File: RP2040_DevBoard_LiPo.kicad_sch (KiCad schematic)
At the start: 56 parts, among them J1 USB_C_Receptacle_USB2.0, J2 Conn_01x18, J3 Conn_01x18, SW1 SW_Push, SW2 SW_Push, U1 W25Q128JVS, U2 USBLC6-2SC6, U3 RP2040, Y1 Crystal_GND23

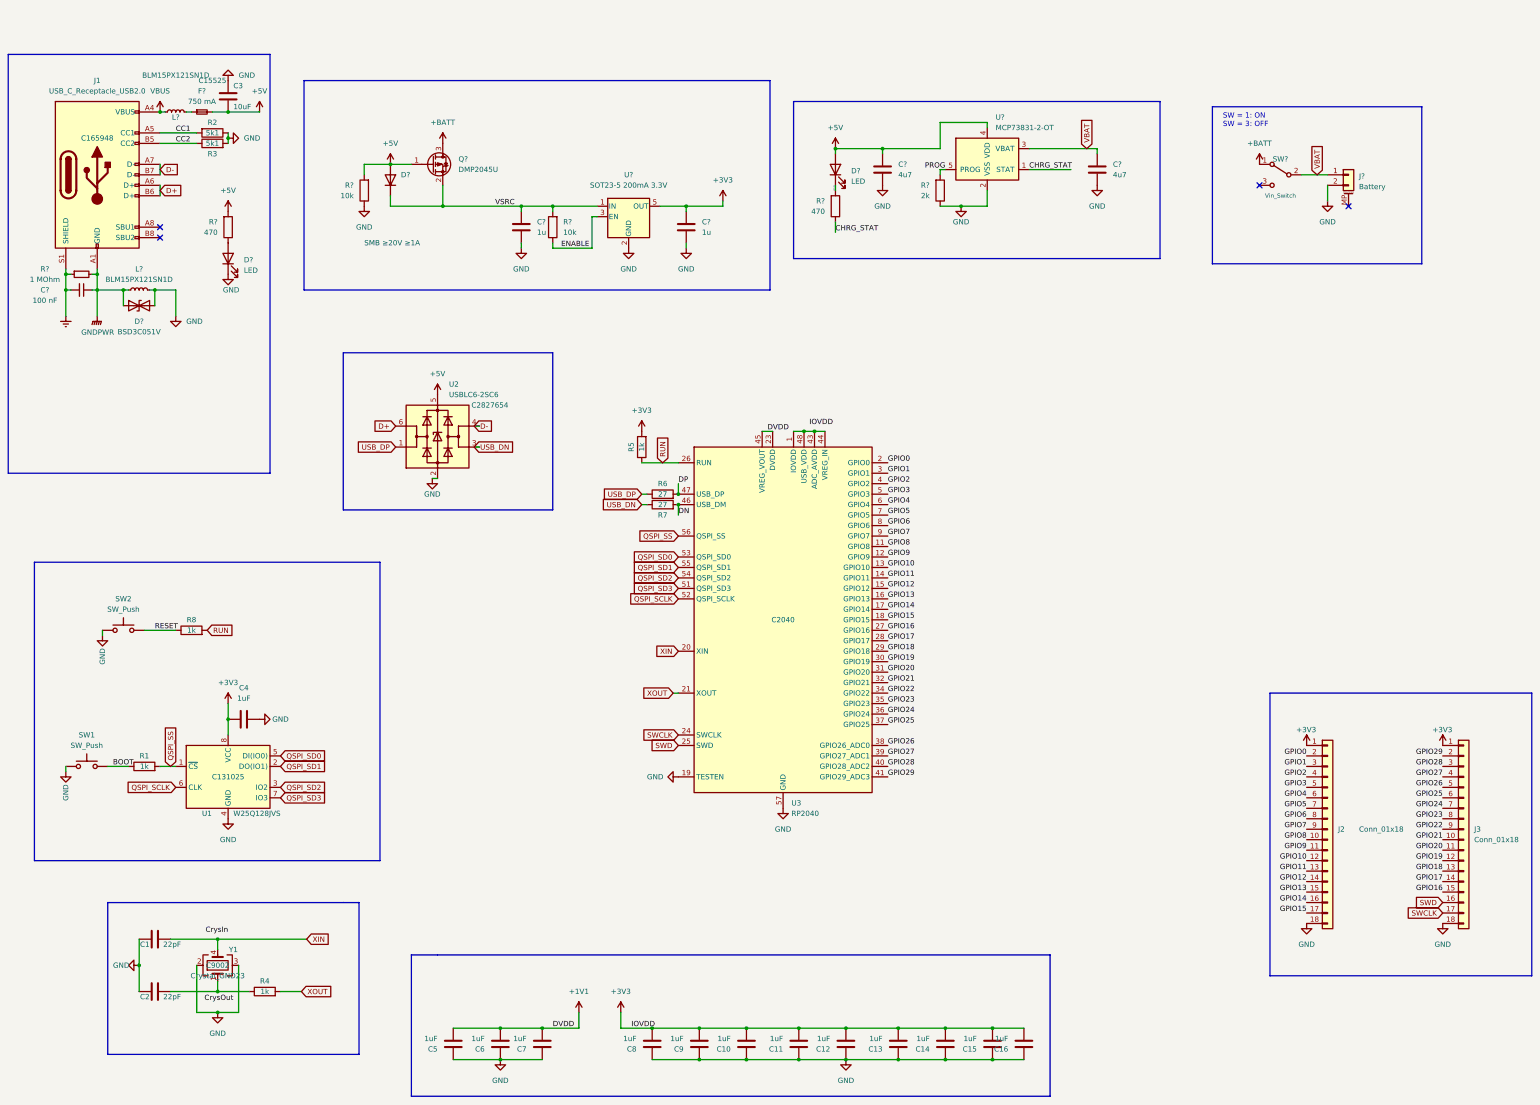
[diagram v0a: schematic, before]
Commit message: added missing 3v3 arrow, changed some footprints
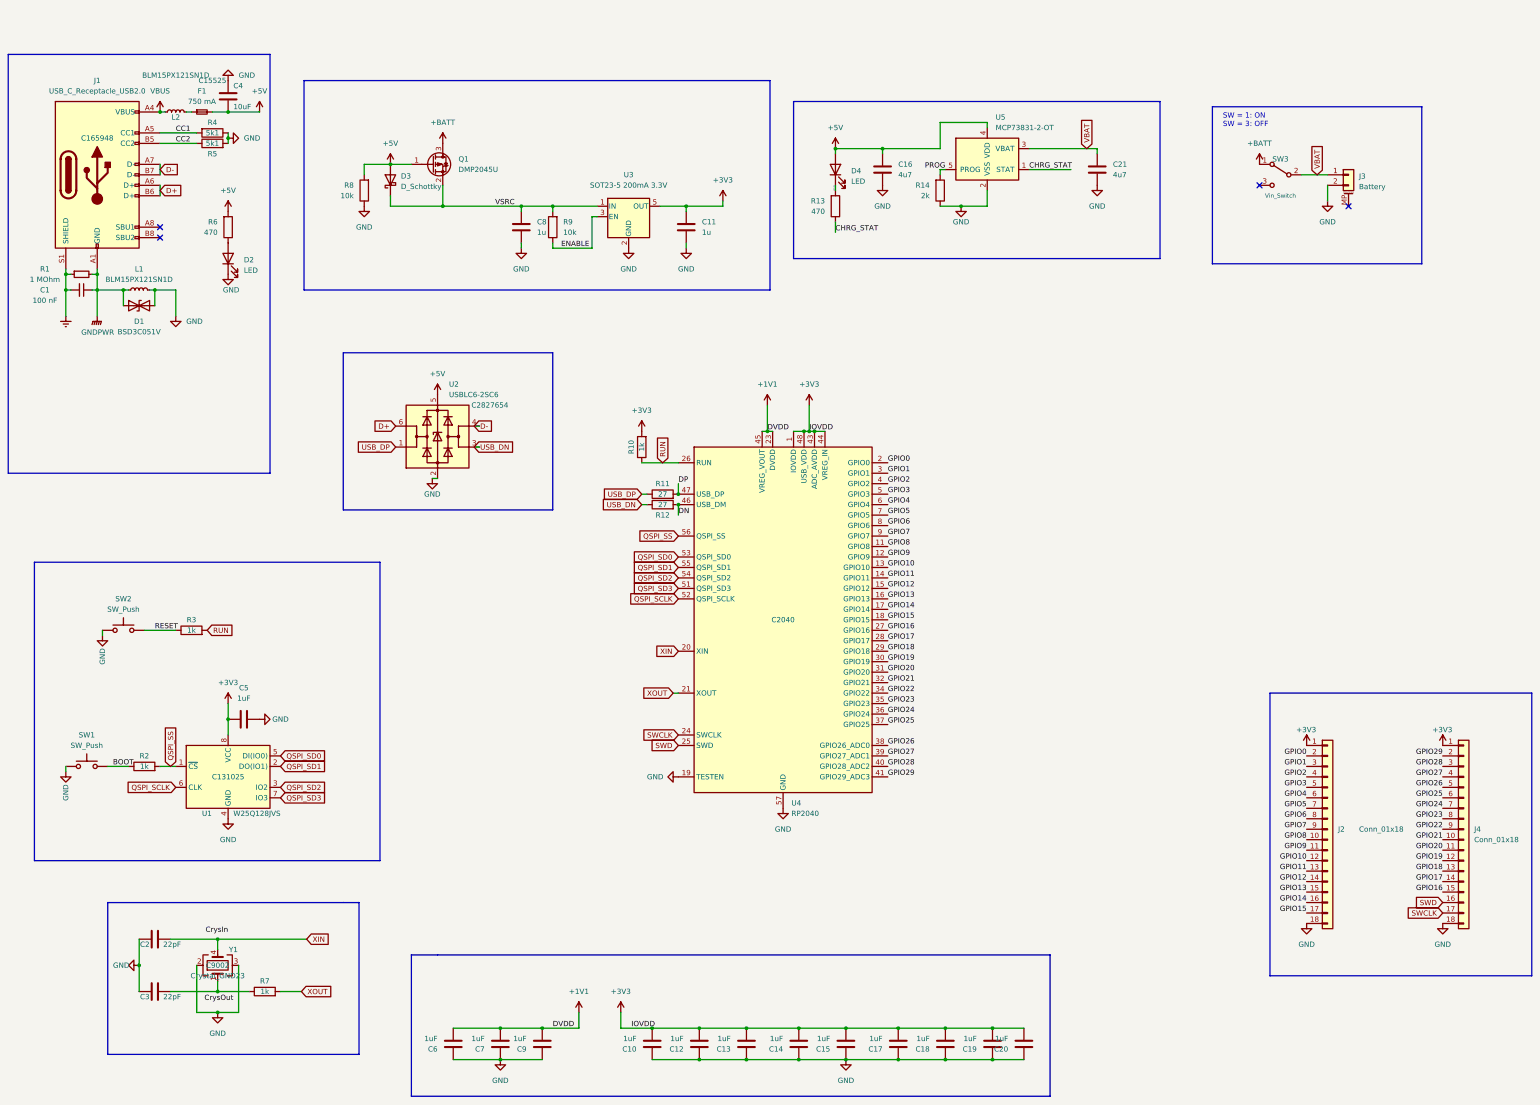
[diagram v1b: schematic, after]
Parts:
- removed D?: SMB ≥20V ≥1A, Diode_SMD:D_1206_3216Metric_Pad1.42x1.75mm_HandSolder, symbol Device:D
- added D3: D_Schottky, Diode_SMD:D_0603_1608Metric, symbol Device:D_Schottky
- C1: renamed from C?; footprint Capacitor_SMD:C_0402_1005Metric -> Diode_SMD:D_0603_1608Metric
- C11, C16, C21, C8: renamed from C?; footprint Capacitor_SMD:C_0805_2012Metric_Pad1.18x1.45mm_HandSolder -> Capacitor_SMD:C_0603_1608Metric
- D2: renamed from D?; footprint (none) -> LED_SMD:LED_0603_1608Metric
- L1, L2: renamed from L?; footprint Inductor_SMD:L_0402_1005Metric -> Inductor_SMD:L_0603_1608Metric
- R1: renamed from R?; footprint Resistor_SMD:R_0402_1005Metric -> Resistor_SMD:R_0603_1608Metric
- R13, R14, R6, R8, R9: renamed from R?; footprint Resistor_SMD:R_0805_2012Metric_Pad1.20x1.40mm_HandSolder -> Resistor_SMD:R_0603_1608Metric
- SW3: renamed from SW?; footprint Buggy_Footprints:1101M2S3CQE2 -> Buggy_Footprints:switch123
- gave numbers to parts that had none: 7
- renumbered C8 to C10, C9 to C12, C10 to C13, C11 to C14, C12 to C15, C13 to C17, C14 to C18, C15 to C19, C1 to C2, C16 to C20, C2 to C3, C3 to C4, C4 to C5, C5 to C6, C6 to C7, C7 to C9, J3 to J4, R5 to R10, R6 to R11, R7 to R12, R1 to R2, R8 to R3, R2 to R4, R3 to R5, R4 to R7, U3 to U4
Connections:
- net +3V3: now also U4.1 (IOVDD), U4.10 (IOVDD), U4.22 (IOVDD), U4.33 (IOVDD), U4.42 (IOVDD), U4.43 (ADC_AVDD), U4.44 (VREG_IN), U4.48 (USB_VDD), U4.49 (IOVDD)
- net +5V: now also D3.2 (A)
- net VSRC: now also D3.1 (K)

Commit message: Updated Schematic. Added LCSC part for most parts
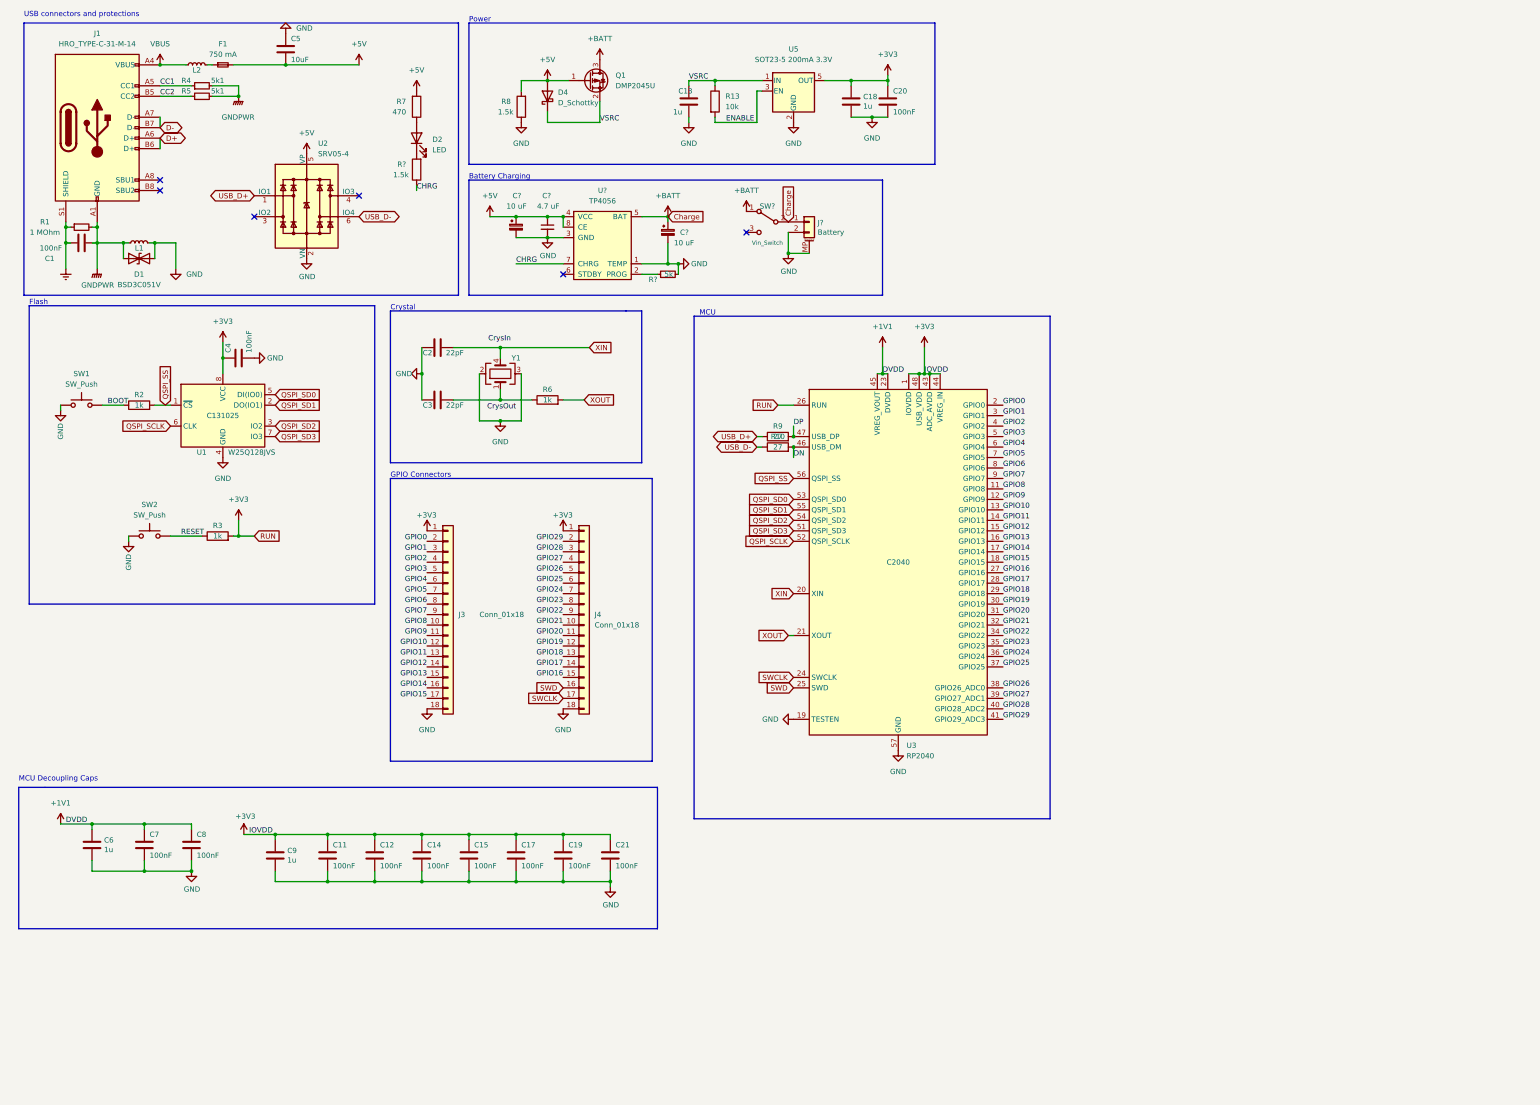
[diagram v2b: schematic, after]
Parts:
- removed C1: 100 nF, Diode_SMD:D_0603_1608Metric, symbol Device:C_Small
- removed C10: 1uF, Capacitor_SMD:C_0603_1608Metric, symbol Device:C
- removed C16: 4u7, Capacitor_SMD:C_0603_1608Metric, symbol Device:C
- removed D4: LED, LED_SMD:LED_0805_2012Metric_Pad1.15x1.40mm_HandSolder, symbol Device:LED
- removed J3: Battery, Connector_JST:JST_PH_S2B-PH-SM4-TB_1x02-1MP_P2.00mm_Horizontal, symbol Connector_Generic_MountingPin:Conn_01x02_MountingPin
- removed R12: 27, Resistor_SMD:R_0603_1608Metric, symbol Device:R
- removed R14: 2k, Resistor_SMD:R_0603_1608Metric, symbol Device:R
- removed R4, R5: 5k1, Resistor_SMD:R_0603_1608Metric, symbol Device:R
- removed R7: 1k, Resistor_SMD:R_0603_1608Metric, symbol Device:R
- removed R9: 10k, Resistor_SMD:R_0603_1608Metric, symbol Device:R
- removed SW3: Vin_Switch, Buggy_Footprints:switch123, symbol Switch:SW_SPDT
- removed U2: USBLC6-2SC6, Package_TO_SOT_SMD:SOT-23-6, symbol Power_Protection:USBLC6-2SC6
- removed U5: MCP73831-2-OT, Package_TO_SOT_SMD:SOT-23-5, symbol Battery_Management:MCP73831-2-OT
- added C1: 100nF, Capacitor_SMD:C_0402_1005Metric, symbol Device:C
- added C? (x2): 10 uF, Capacitor_SMD:CP_Elec_3x5.3, symbol Device:C_Polarized_Small
- added C?: 4.7 uF, Capacitor_SMD:C_0402_1005Metric, symbol Device:C_Small
- added J?: Battery, Connector_JST:JST_PH_S2B-PH-K_1x02_P2.00mm_Horizontal, symbol Connector_Generic_MountingPin:Conn_01x02_MountingPin
- added R4, R5: 5k1, Resistor_SMD:R_0402_1005Metric, symbol Device:R_Small
- added R6: 1k, Resistor_SMD:R_0402_1005Metric, symbol Device:R
- added R?: 5k, Resistor_SMD:R_0603_1608Metric, symbol Device:R_Small
- added R?: 1.5k, Resistor_SMD:R_0402_1005Metric, symbol Device:R
- added SW?: Vin_Switch, Buggy_Footprints:switch123, symbol Switch:SW_SPDT
- added U2: SRV05-4, Package_TO_SOT_SMD:SOT-23-6, symbol Power_Protection:SRV05-4
- added U?: TP4056, Package_SO:SOP-8-1EP_4.57x4.57mm_P1.27mm_EP4.57x4.45mm, symbol marbastlib-various:TP4056
- C11, C8: value 1u -> 100nF; footprint Capacitor_SMD:C_0603_1608Metric -> Capacitor_SMD:C_0402_1005Metric; LCSC (none) -> C1525
- C12, C14, C15, C17, C19, C20, C7: value 1uF -> 100nF; footprint Capacitor_SMD:C_0603_1608Metric -> Capacitor_SMD:C_0402_1005Metric; LCSC C52923 -> C1525
- C13, C18, C6, C9: value 1uF -> 1u; footprint Capacitor_SMD:C_0603_1608Metric -> Capacitor_SMD:C_0402_1005Metric; LCSC C52923 -> C14445; pin (none) -> 44
- C2, C3: footprint Capacitor_SMD:C_0603_1608Metric -> Capacitor_SMD:C_0402_1005Metric; LCSC C1555 -> C70464
- C21: value 4u7 -> 100nF; footprint Capacitor_SMD:C_0603_1608Metric -> Capacitor_SMD:C_0402_1005Metric; LCSC (none) -> C1525
- C4: value 10uF -> 100nF; footprint Capacitor_SMD:C_0603_1608Metric -> Capacitor_SMD:C_0402_1005Metric; LCSC C15525 -> C1525
- C5: value 1uF -> 10uF; footprint Capacitor_SMD:C_0603_1608Metric -> Capacitor_SMD:C_0402_1005Metric; LCSC C52923 -> C15525
- D1: LCSC (none) -> C151996
- D2: footprint LED_SMD:LED_0603_1608Metric -> LED_SMD:LED_1206_3216Metric; LCSC (none) -> C434443
- D4: renamed from D3; footprint Diode_SMD:D_0603_1608Metric -> Diode_SMD:D_SOD-323; LCSC (none) -> C22624
- F1: LCSC (none) -> C182438
- J1: value USB_C_Receptacle_USB2.0 -> HRO_TYPE-C-31-M-14
- L1, L2: footprint Inductor_SMD:L_0603_1608Metric -> Inductor_SMD:L_0402_1005Metric; LCSC (none) -> C88970
- Q1: LCSC (none) -> C347476
- R1: footprint Resistor_SMD:R_0603_1608Metric -> Resistor_SMD:R_0402_1005Metric; LCSC (none) -> C26083
- R10: value 1k -> 27; footprint Resistor_SMD:R_0603_1608Metric -> Resistor_SMD:R_0402_1005Metric; LCSC (none) -> C3017455
- R13: value 470 -> 10k; footprint Resistor_SMD:R_0603_1608Metric -> Resistor_SMD:R_0402_1005Metric; LCSC (none) -> C60490
- R2, R3: footprint Resistor_SMD:R_0603_1608Metric -> Resistor_SMD:R_0402_1005Metric; LCSC (none) -> C106235
- R7: renamed from R6; footprint Resistor_SMD:R_0603_1608Metric -> Resistor_SMD:R_0402_1005Metric; LCSC (none) -> C25117
- R8: value 10k -> 1.5k; footprint Resistor_SMD:R_0603_1608Metric -> Resistor_SMD:R_0402_1005Metric; LCSC (none) -> C114759
- R9: renamed from R11; footprint Resistor_SMD:R_0603_1608Metric -> Resistor_SMD:R_0402_1005Metric; LCSC C25190 -> C3017455
- U5: renamed from U3; LCSC (none) -> C11337
- renumbered J2 to J3, U4 to U3
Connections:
- net CHRG_STAT is gone; now on net VSRC: R13.1
- net LED_D2 is gone; now on net ENABLE: R13.2
- net VBAT is gone; now on net GND: C21.1
- net +1V1: now also C6.1, C8.2; no longer C6.2, C9.2
- net +3V3: now also C18.1, C21.2, C4.2, C9.1, R3.2, U3.26 (RUN); no longer C13.2, C18.2, C5.2, R10.2
- net +5V: now also C5.2, C?.1, C?.1, U2.5 (VP), U?.4 (VCC), U?.8 (CE); no longer C4.2
- net +BATT: now also C?.1, J?.1 (Pin_1), SW?.1 (A), SW?.2 (B), U?.5 (BAT)
- net CC1: now also R4.1
- net CC2: now also R5.1
- net DN: now also R10.2
- net Earth: now also C1.1
- net GND: now also C13.2, C18.2, C6.2, C8.1, C9.2, C?.2, C?.2, C?.2, J?.2 (Pin_2), J?.MP (MountPin), R?.2, U2.2 (VN), U?.1 (TEMP), U?.3 (GND); no longer C13.1, C18.1, C21.2, C6.1, C8.2, C9.1, D2.1 (K)
- net GNDPWR: now also C1.2, R4.2, R5.2
- net VSRC: now also C13.1; no longer C8.1
- net XOUT: now also R6.2
- net at C3.1, Y1.1: now also R6.1
- removed net RUN: R10.1, R3.2, U3.26 (RUN)
- net USB_DP renamed USB_D+
- net USB_D+: now also U2.1 (IO1)
- new net: R?.1, U?.2 (PROG)
- new net: D2.1 (K), R?.2
- new net CHRG: R?.1, U?.7 (CHRG)
- new net USB_D-: R10.1, U2.6 (IO4)
- no-connect marks 4 -> 6
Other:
- note added: "Battery Charging"
- note added: "Crystal"
- note added: "Flash"
- note added: "GPIO Connectors"
- note added: "MCU"
- note added: "MCU Decoupling Caps"
- note added: "Power"
- note added: "USB connectors and protections"
- note removed: "SW = 1: ON SW = 3: OFF"
- moved on the sheet: D2, D4, J3, J4, Q1, R3, R7, R8, R9, SW1, SW2, U1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

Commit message: started routing
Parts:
- removed D2: LED, LED_SMD:LED_1206_3216Metric, symbol Device:LED
- removed J?: Battery, Connector_JST:JST_PH_S2B-PH-K_1x02_P2.00mm_Horizontal, symbol Connector_Generic_MountingPin:Conn_01x02_MountingPin
- removed R7: 470, Resistor_SMD:R_0402_1005Metric, symbol Device:R
- removed U2: SRV05-4, Package_TO_SOT_SMD:SOT-23-6, symbol Power_Protection:SRV05-4
- added D4: LED, LED_SMD:LED_1206_3216Metric, symbol Device:LED
- added J4: Battery, Connector_JST:JST_EH_S2B-EH_1x02_P2.50mm_Horizontal, symbol Connector_Generic:Conn_01x02
- added R9: 470, Resistor_SMD:R_0402_1005Metric, symbol Device:R
- added U1: USBLC6-2SC6, Package_TO_SOT_SMD:SOT-23-6, symbol Power_Protection:USBLC6-2SC6
- gave numbers to parts that had none: 7
- renumbered C2 to C10, C3 to C11, C6 to C12, C7 to C13, C8 to C14, C9 to C15, C11 to C16, C12 to C17, C14 to C18, C15 to C19, C5 to C2, C17 to C20, C19 to C21, C21 to C22, C4 to C3, C13 to C4, C18 to C5, C20 to C6, D4 to D3, J3 to J2, J4 to J3, R6 to R12, R9 to R13, R10 to R14, R4 to R2, R5 to R3, R2 to R5, R3 to R6, R8 to R7, R13 to R8, U1 to U2, U5 to U3, U3 to U5
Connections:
- net +5V: now also R9.2, U1.5 (VBUS)
- net +BATT: now also J4.1 (Pin_1)
- net CHRG: no longer R10.1, U4.7 (CHRG)
- net D+: now also U1.1 (I/O1)
- net D-: now also U1.3 (I/O2)
- net GND: now also J4.2 (Pin_2), U1.2 (GND)
- net USB_D+: now also U1.6 (I/O1)
- net USB_D-: now also U1.4 (I/O2)
- net at R10.2: now also D4.1 (K)
- new net: R10.1, U4.7 (CHRG)
- new net: D4.2 (A), R9.1
- no-connect marks 6 -> 4
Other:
- moved on the sheet: C1, C10, C11, C12, C13, C14, C15, C16, C17, C18, C19, C2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
